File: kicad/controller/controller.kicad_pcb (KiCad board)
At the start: 2 copper layers, 52 x 29 mm, 42 parts, among them J1 JST_BAT, J2 JST_BOOKMARK, J3 CONN_UPDI, J4 UART_DBG, Q1 DMP1045U, SW1 SW_DIP_x01, U1 DS3231, U2 TP4056, U3 ATTINY1616

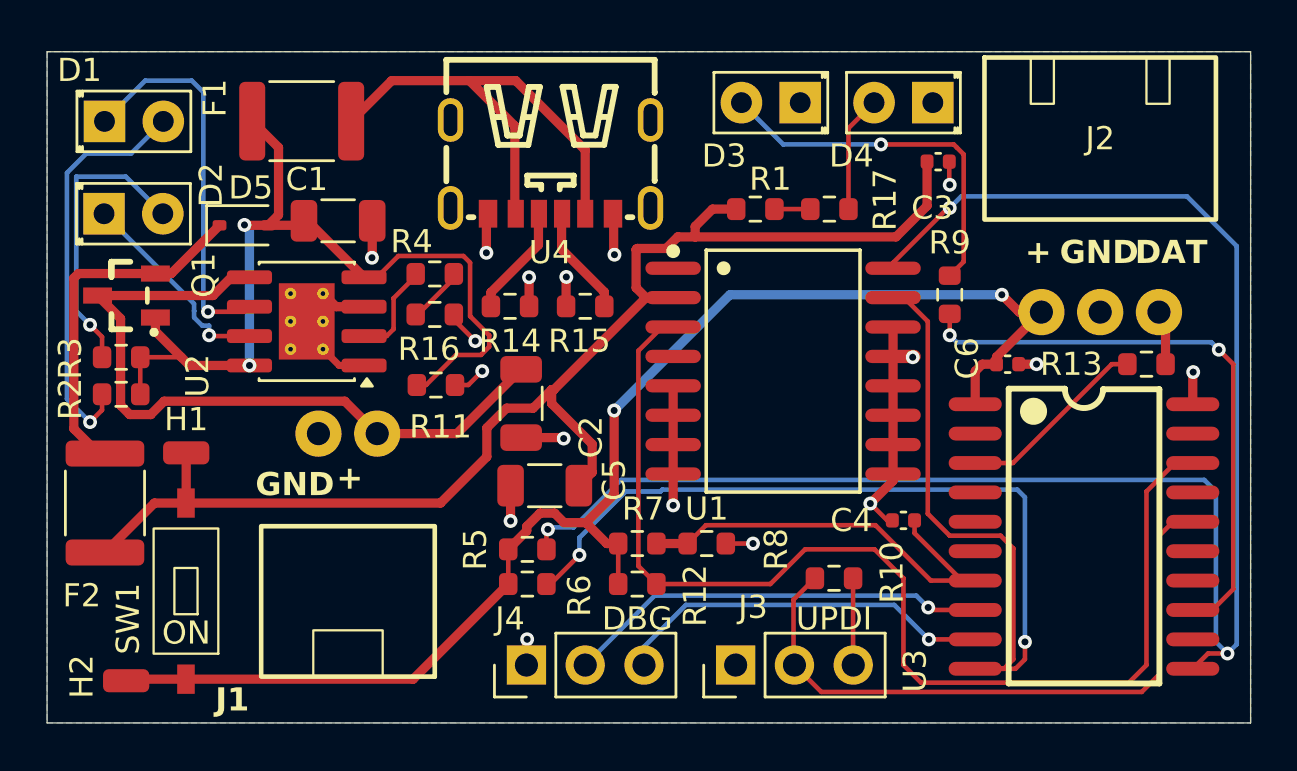
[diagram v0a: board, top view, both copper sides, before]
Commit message: clean up position of footprints
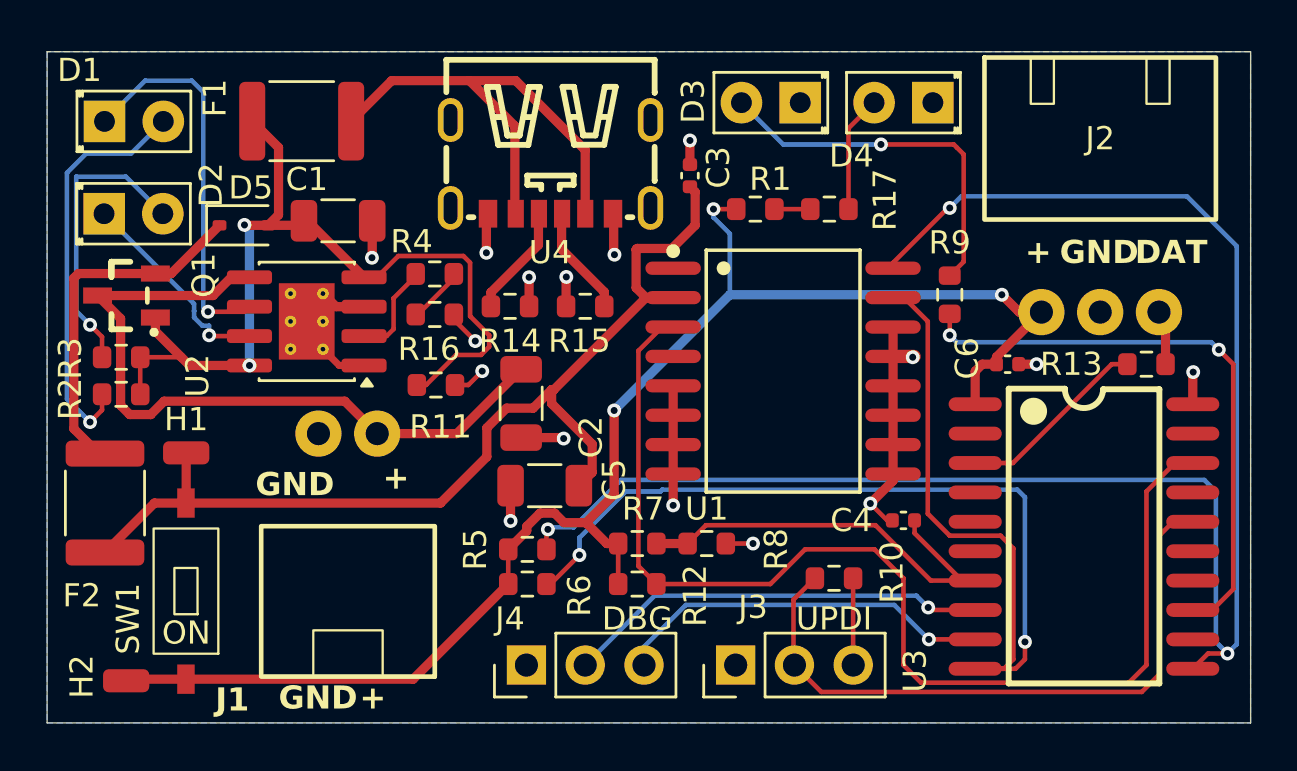
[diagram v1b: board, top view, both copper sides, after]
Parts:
- moved C3 10.7 mm to (42.8, 20.4), turned to 90 degrees
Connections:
- R1 pad 1: Net-(U1A-VCC) -> Net-(J2-VIN)
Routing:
- net Net-(U1A-VCC): track 57.3 -> 44.2 mm
- net Net-(J2-VIN): track 60.1 -> 65.1 mm, vias 2 -> 3
- net GND: track 38.3 -> 37.2 mm, vias 17 -> 16

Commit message: change usb C footprint to USB-TYPE-C-006 https://jlcpcb.com/partdetail/DEALON-USB_TYPE_C006/C2927026
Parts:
- U4: footprint custom-footprints:TYPE-C-SMD_TYPE-C-6P -> custom-footprints:USB-C-SMD_USB-TYPE-C-006
- moved C3 8.78 mm to (39.5, 28.5), turned to -90 degrees
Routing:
- net GND: track 37.2 -> 45.8 mm
- net Net-(U1A-VCC): track 44.2 -> 38.9 mm
